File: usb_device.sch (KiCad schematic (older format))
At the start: 9 parts, among them J3 USB_C_Receptacle, U6 USB6B1, U7 USB6B1

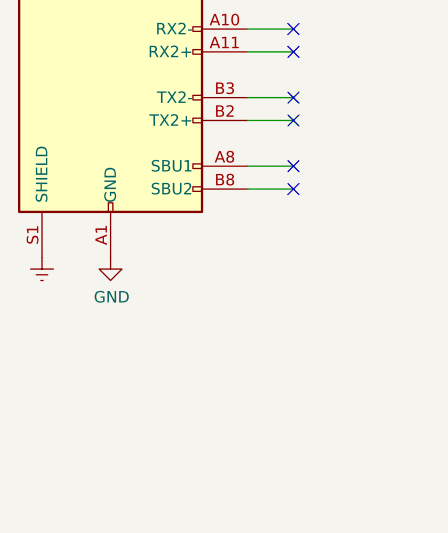
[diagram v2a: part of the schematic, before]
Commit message: Supply caps, initial signal states and headers
  * Added bulk supply caps.
  * Set initial control signal states via resistors.
  * Add debug headers.
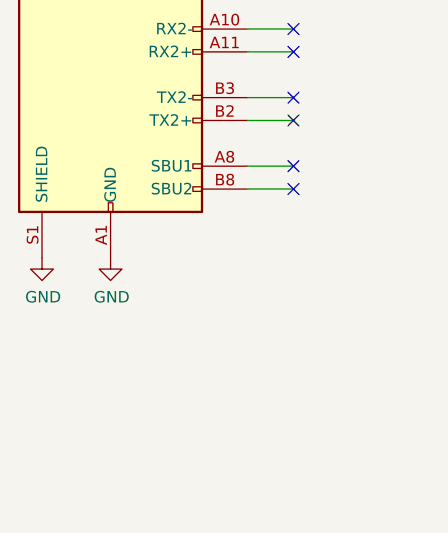
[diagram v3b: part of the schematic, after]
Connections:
- net Earth is gone; now on net GND: J3.S1 (SHIELD)
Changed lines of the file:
@@
 AR Path="/61B0D0F9/61B10DD4" Ref="#PWR012"  Part="1"
 AR Path="/61AFE355/61B10DD4" Ref="#PWR062"  Part="1"
-F 0 "#PWR012" H 2600 4350 50  0001 C CNN
+F 0 "#PWR062" H 2600 4350 50  0001 C CNN
 F 1 "GND" H 2605 4427 50  0000 C CNN
 F 2 "" H 2600 4600 50  0001 C CNN
 F 3 "" H 2600 4600 50  0001 C CNN
 	1    2600 4600
-	1    0    0    -1
-$EndComp
-$Comp
-L power:Earth #PWR?
-U 1 1 61B10DDA
-P 2300 4600
-AR Path="/61B10DDA" Ref="#PWR?"  Part="1"
-AR Path="/61B0D0F9/61B10DDA" Ref="#PWR011"  Part="1"
-AR Path="/61AFE355/61B10DDA" Ref="#PWR061"  Part="1"
-F 0 "#PWR011" H 2300 4350 50  0001 C CNN
-F 1 "Earth" H 2300 4450 50  0001 C CNN
-F 2 "" H 2300 4600 50  0001 C CNN
-F 3 "~" H 2300 4600 50  0001 C CNN
-	1    2300 4600
 	1    0    0    -1
 $EndComp
@@
 AR Path="/61B0D0F9/61B17220" Ref="#PWR013"  Part="1"
 AR Path="/61AFE355/61B17220" Ref="#PWR063"  Part="1"
-F 0 "#PWR013" H 5550 2100 50  0001 C CNN
+F 0 "#PWR063" H 5550 2100 50  0001 C CNN
 F 1 "GND" H 5555 2177 50  0000 C CNN
 F 2 "" H 5550 2350 50  0001 C CNN
@@
 AR Path="/61B0D0F9/61B174BC" Ref="#PWR014"  Part="1"
 AR Path="/61AFE355/61B174BC" Ref="#PWR064"  Part="1"
-F 0 "#PWR014" H 6300 2100 50  0001 C CNN
+F 0 "#PWR064" H 6300 2100 50  0001 C CNN
 F 1 "GND" H 6305 2177 50  0000 C CNN
 F 2 "" H 6300 2350 50  0001 C CNN
@@
 AR Path="/61B0D0F9/61B36C9F" Ref="#PWR016"  Part="1"
 AR Path="/61AFE355/61B36C9F" Ref="#PWR066"  Part="1"
-F 0 "#PWR016" H 7100 3650 50  0001 C CNN
+F 0 "#PWR066" H 7100 3650 50  0001 C CNN
 F 1 "GND" H 7105 3727 50  0000 C CNN
 F 2 "" H 7100 3900 50  0001 C CNN
@@
 	1    0    0    -1
 $EndComp
-Text Label 7300 3150 0    50   ~ 0
-VBUS
-Wire Wire Line
-	7300 3150 7100 3150
-Wire Wire Line
-	7100 3150 7100 3250
 Wire Wire Line
 	7100 3850 7100 3900
@@
 AR Path="/61B0D0F9/61BB6C17" Ref="#PWR015"  Part="1"
 AR Path="/61AFE355/61BB6C17" Ref="#PWR065"  Part="1"
-F 0 "#PWR015" H 7050 5250 50  0001 C CNN
+F 0 "#PWR065" H 7050 5250 50  0001 C CNN
 F 1 "GND" H 7055 5327 50  0000 C CNN
 F 2 "" H 7050 5500 50  0001 C CNN
@@
 	1    0    0    -1
 $EndComp
-Text Label 7250 4750 0    50   ~ 0
-VBUS
-Wire Wire Line
-	7250 4750 7050 4750
-Wire Wire Line
-	7050 4750 7050 4850
 Wire Wire Line
 	7050 5450 7050 5500
@@
 Wire Wire Line
 	7500 3650 7650 3650
+Wire Wire Line
+	7050 4750 7050 4850
+Wire Wire Line
+	7250 4750 7050 4750
+Text Label 7250 4750 0    50   ~ 0
+VBUS
+Wire Wire Line
+	7100 3150 7100 3250
+Wire Wire Line
+	7300 3150 7100 3150
+Text Label 7300 3150 0    50   ~ 0
+VBUS
+$Comp
+L power:GND #PWR?
+U 1 1 61AD16C9
+P 2300 4600
+AR Path="/61AD16C9" Ref="#PWR?"  Part="1"
+AR Path="/61B0D0F9/61AD16C9" Ref="#PWR0192"  Part="1"
+AR Path="/61AFE355/61AD16C9" Ref="#PWR0193"  Part="1"
+F 0 "#PWR0193" H 2300 4350 50  0001 C CNN
+F 1 "GND" H 2305 4427 50  0000 C CNN
+F 2 "" H 2300 4600 50  0001 C CNN
+F 3 "" H 2300 4600 50  0001 C CNN
+	1    2300 4600
+	1    0    0    -1
+$EndComp
 $EndSCHEMATC

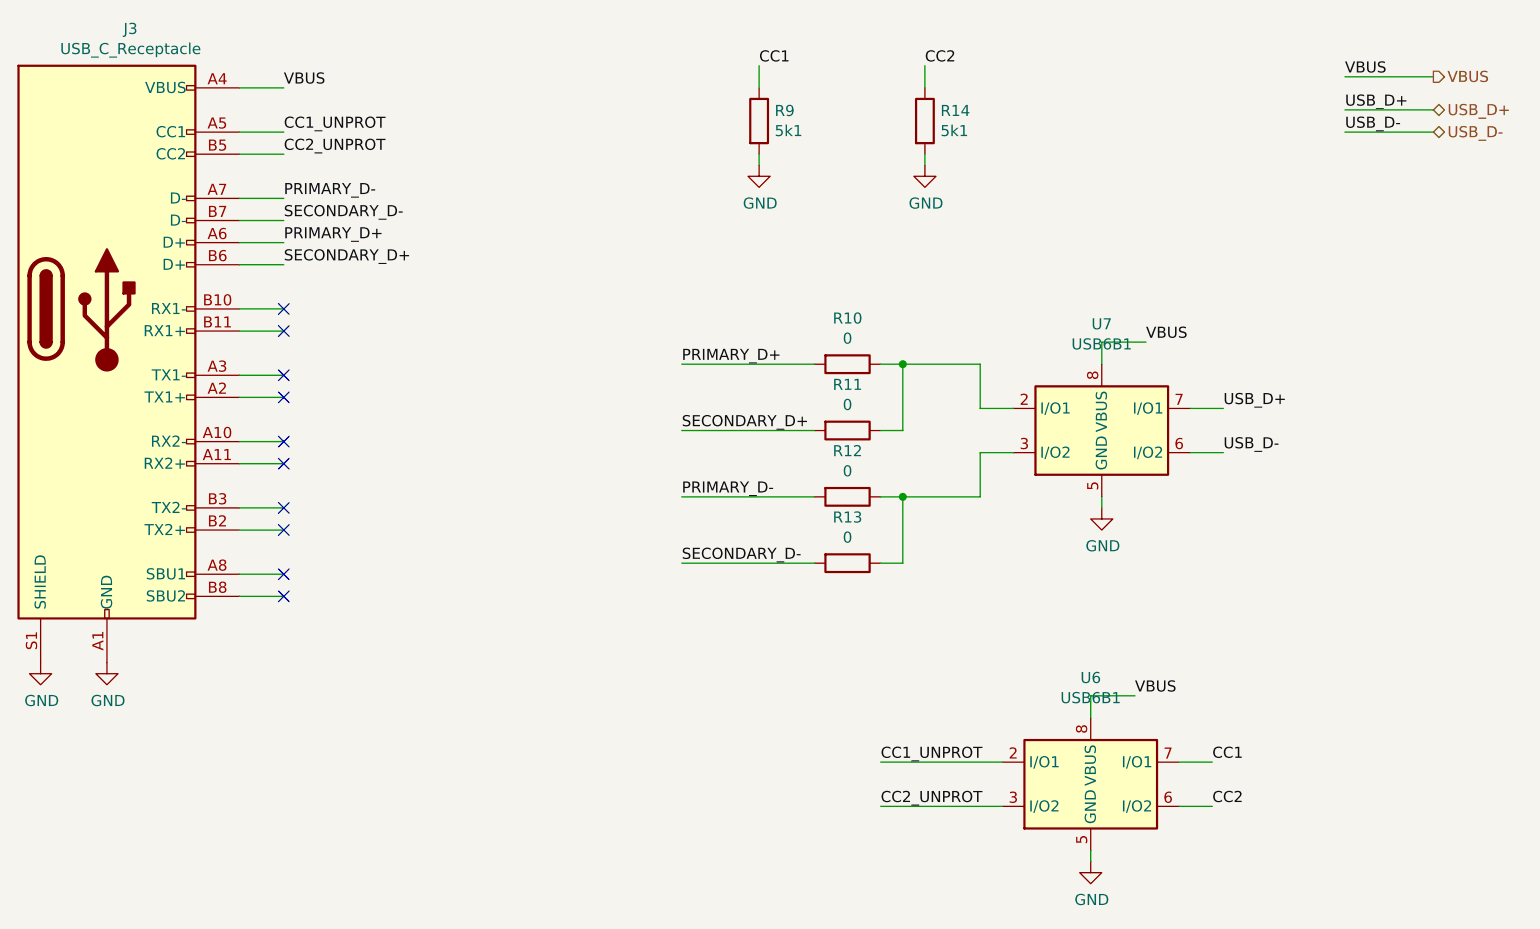
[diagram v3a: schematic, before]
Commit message: Replace MCU by something available in distributors
Given the current chip shortage the STM32F0 was not available from
JLCPCB. This one (STM32F411CE) is available in large quantities from
JLCPCB. Despite being much more powerful than the F0, it is still in the
price range and actually cheaper than the STM32F103C8T6... which I don't
understand...
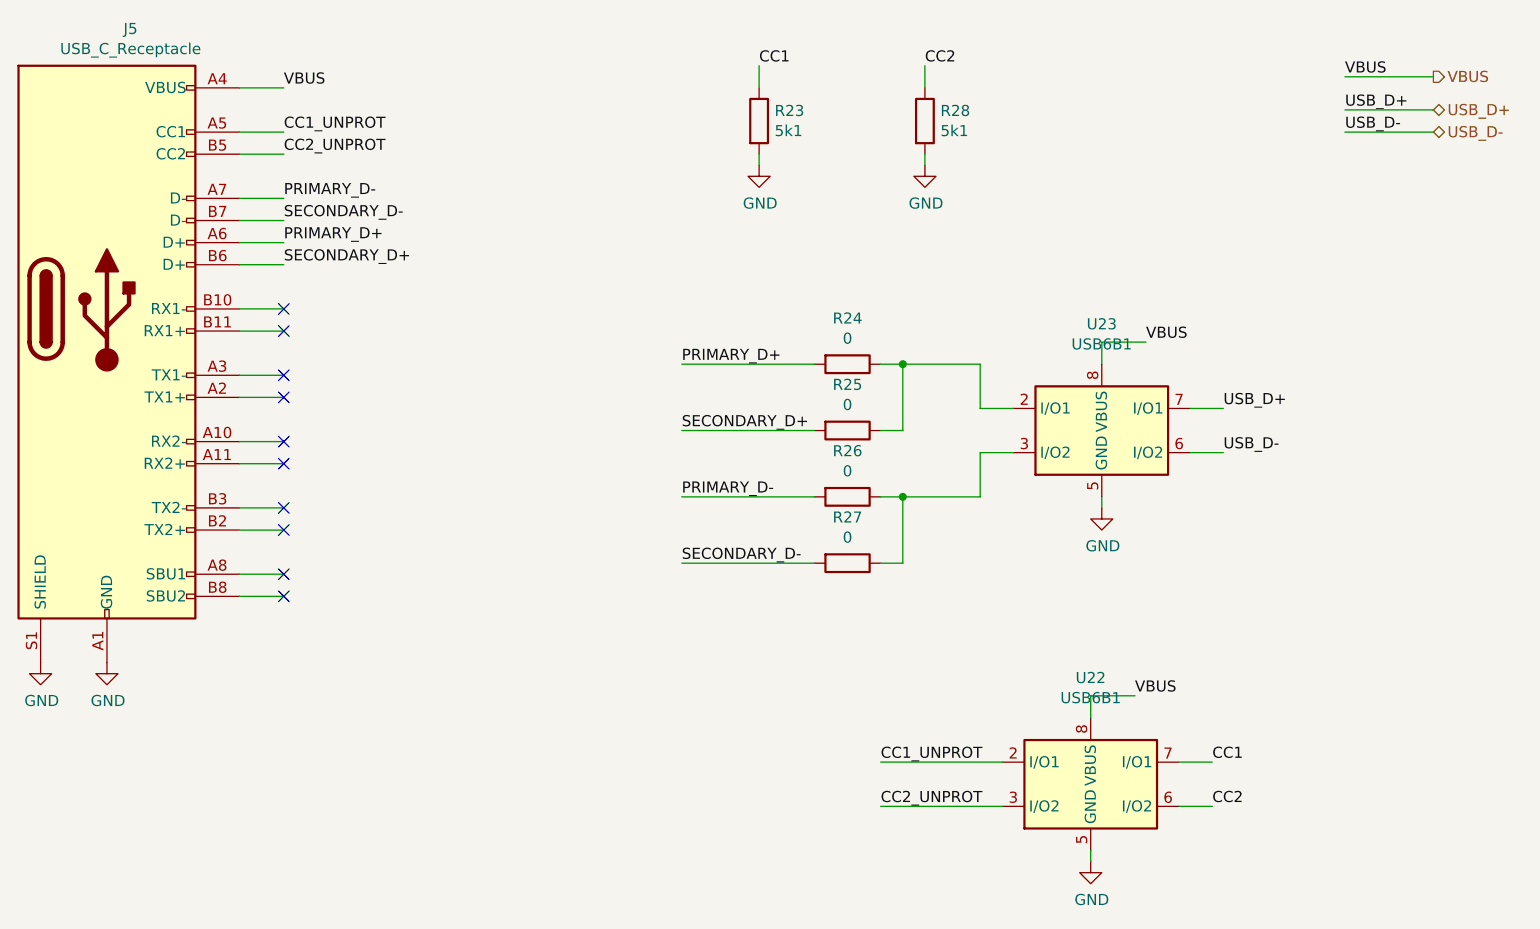
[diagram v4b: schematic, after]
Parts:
- U6, U7: LCSC (none) -> C10508
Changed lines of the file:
@@
 $Descr A4 11693 8268
 encoding utf-8
-Sheet 3 12
+Sheet 11 12
 Title "USB Whisperer"
 Date "2021-11-21"
@@
 AR Path="/61B0D0F9/61B10DC4" Ref="J3"  Part="1"
 AR Path="/61AFE355/61B10DC4" Ref="J5"  Part="1"
-F 0 "J3" H 2707 4267 50  0000 C CNN
+F 0 "J5" H 2707 4267 50  0000 C CNN
 F 1 "USB_C_Receptacle" H 2707 4176 50  0000 C CNN
 F 2 "" H 2750 3000 50  0001 C CNN
@@
 AR Path="/61B0D0F9/61B166FB" Ref="R9"  Part="1"
 AR Path="/61AFE355/61B166FB" Ref="R23"  Part="1"
-F 0 "R9" H 5620 2196 50  0000 L CNN
+F 0 "R23" H 5620 2196 50  0000 L CNN
 F 1 "5k1" H 5620 2105 50  0000 L CNN
 F 2 "" V 5480 2150 50  0001 C CNN
@@
 AR Path="/61B0D0F9/61B16DA0" Ref="R14"  Part="1"
 AR Path="/61AFE355/61B16DA0" Ref="R28"  Part="1"
-F 0 "R14" H 6370 2196 50  0000 L CNN
+F 0 "R28" H 6370 2196 50  0000 L CNN
 F 1 "5k1" H 6370 2105 50  0000 L CNN
 F 2 "" V 6230 2150 50  0001 C CNN
@@
 AR Path="/61B0D0F9/61B1833D" Ref="R10"  Part="1"
 AR Path="/61AFE355/61B1833D" Ref="R24"  Part="1"
-F 0 "R10" V 5743 3250 50  0000 C CNN
+F 0 "R24" V 5743 3250 50  0000 C CNN
 F 1 "0" V 5834 3250 50  0000 C CNN
 F 2 "" V 5880 3250 50  0001 C CNN
@@
 AR Path="/61B0D0F9/61B18B52" Ref="R11"  Part="1"
 AR Path="/61AFE355/61B18B52" Ref="R25"  Part="1"
-F 0 "R11" V 5743 3550 50  0000 C CNN
+F 0 "R25" V 5743 3550 50  0000 C CNN
 F 1 "0" V 5834 3550 50  0000 C CNN
 F 2 "" V 5880 3550 50  0001 C CNN
@@
 AR Path="/61B0D0F9/61B1BA3B" Ref="R12"  Part="1"
 AR Path="/61AFE355/61B1BA3B" Ref="R26"  Part="1"
-F 0 "R12" V 5743 3850 50  0000 C CNN
+F 0 "R26" V 5743 3850 50  0000 C CNN
 F 1 "0" V 5834 3850 50  0000 C CNN
 F 2 "" V 5880 3850 50  0001 C CNN
@@
 AR Path="/61B0D0F9/61B1BA41" Ref="R13"  Part="1"
 AR Path="/61AFE355/61B1BA41" Ref="R27"  Part="1"
-F 0 "R13" V 5743 4150 50  0000 C CNN
+F 0 "R27" V 5743 4150 50  0000 C CNN
 F 1 "0" V 5834 4150 50  0000 C CNN
 F 2 "" V 5880 4150 50  0001 C CNN
@@
 AR Path="/61B0D0F9/61B30609" Ref="U7"  Part="1"
 AR Path="/61AFE355/61B30609" Ref="U23"  Part="1"
-F 0 "U7" H 7100 4031 50  0000 C CNN
+F 0 "U23" H 7100 4031 50  0000 C CNN
 F 1 "USB6B1" H 7100 3940 50  0000 C CNN
 F 2 "Package_SO:SOIC-8_3.9x4.9mm_P1.27mm" H 7100 3550 50  0001 C CNN
 F 3 "http://www.st.com/content/ccc/resource/technical/document/datasheet/3e/ec/b2/54/b2/76/47/90/CD00001361.pdf/files/CD00001361.pdf/jcr:content/translations/en.CD00001361.pdf" H 6150 3450 50  0001 C CNN
+F 4 "C10508" H 7100 3550 50  0001 C CNN "LCSC"
 	1    7100 3550
 	1    0    0    -1
@@
 AR Path="/61B0D0F9/61BB6C09" Ref="U6"  Part="1"
 AR Path="/61AFE355/61BB6C09" Ref="U22"  Part="1"
-F 0 "U6" H 7050 5631 50  0000 C CNN
+F 0 "U22" H 7050 5631 50  0000 C CNN
 F 1 "USB6B1" H 7050 5540 50  0000 C CNN
 F 2 "Package_SO:SOIC-8_3.9x4.9mm_P1.27mm" H 7050 5150 50  0001 C CNN
 F 3 "http://www.st.com/content/ccc/resource/technical/document/datasheet/3e/ec/b2/54/b2/76/47/90/CD00001361.pdf/files/CD00001361.pdf/jcr:content/translations/en.CD00001361.pdf" H 6100 5050 50  0001 C CNN
+F 4 "C10508" H 7050 5150 50  0001 C CNN "LCSC"
 	1    7050 5150
 	1    0    0    -1
